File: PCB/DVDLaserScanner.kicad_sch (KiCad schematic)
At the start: 4 parts, among them P1 USB_C_Plug_USB2.0, U3 MIC5365-3.3YC5

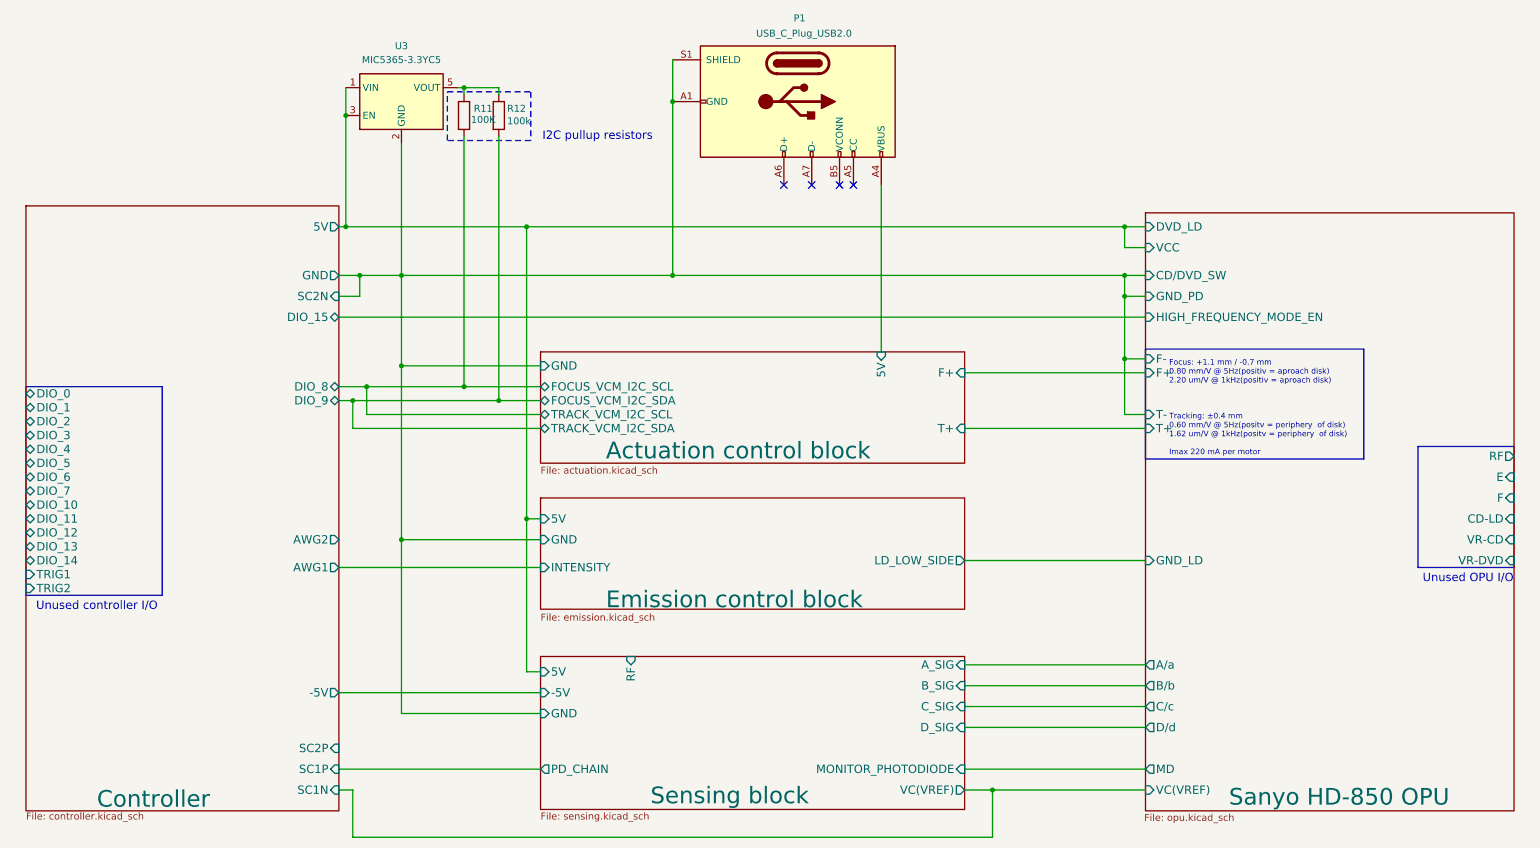
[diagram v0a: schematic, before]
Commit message: Update schematic based on testing
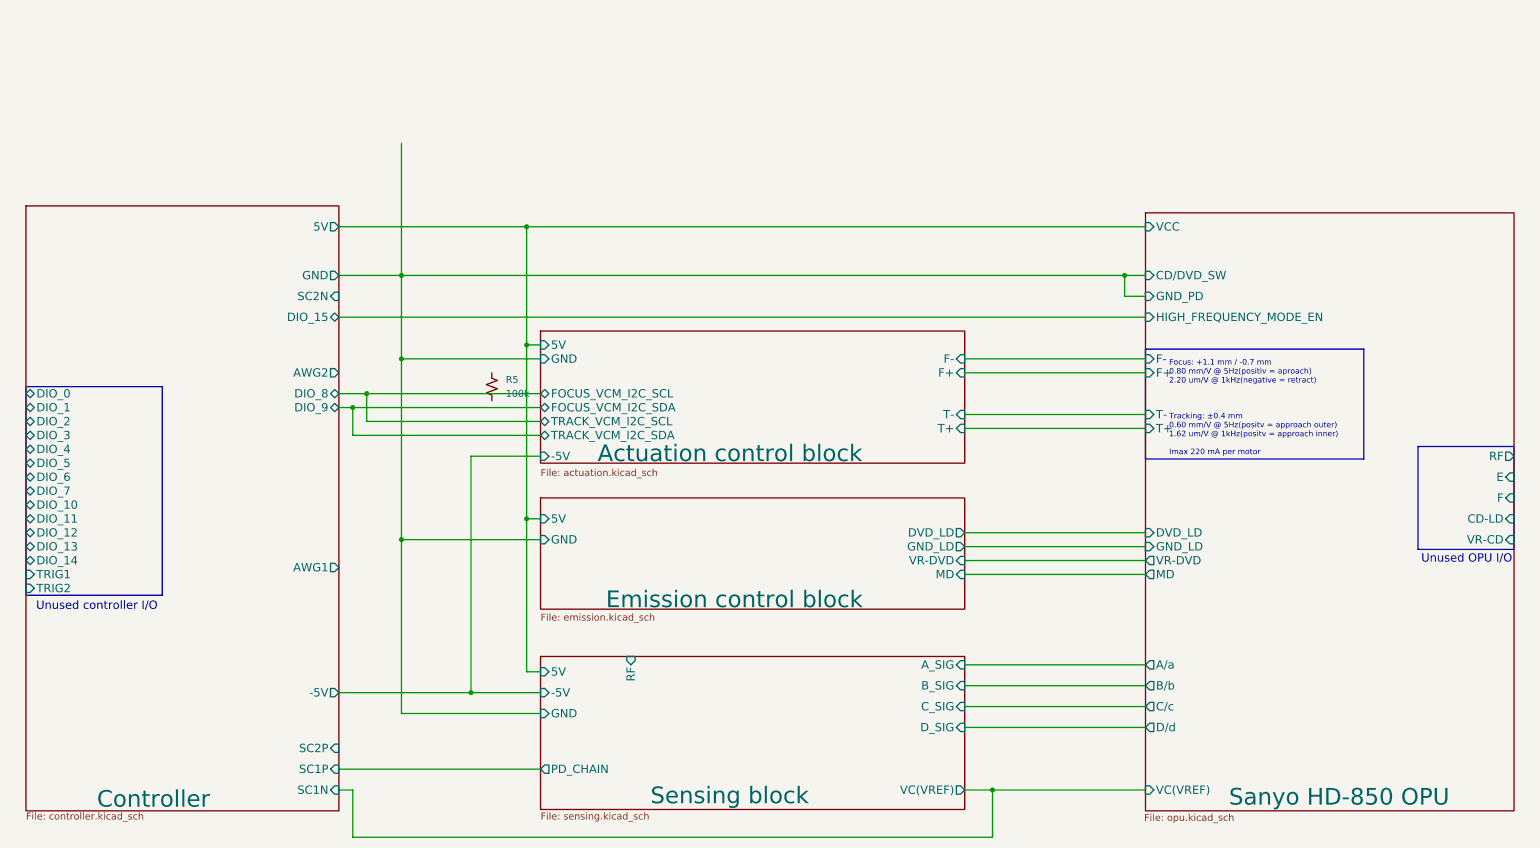
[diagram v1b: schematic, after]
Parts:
- removed P1: USB_C_Plug_USB2.0, symbol Connector:USB_C_Plug_USB2.0
- removed R11: 100K, symbol Device:R
- removed R12: 100k, symbol Device:R
- removed U3: MIC5365-3.3YC5, Package_TO_SOT_SMD:SOT-353_SC-70-5, symbol Regulator_Linear:MIC5365-3.3YC5
- added R5: 100k, symbol Device:R_Small_US
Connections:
- no-connect marks 4 -> 0
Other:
- sheet Actuation control block ports: added -5V, F-, T-; removed none
- sheet Emission control block ports: added DVD_LD, GND_LD, MD, VR-DVD; removed INTENSITY, LD_LOW_SIDE
- sheet Sensing block ports: added none; removed MONITOR_PHOTODIODE
- note added: "Focus: +1.1 mm / -0.7 mm 0.80 mm/V @ 5Hz(positiv = aproach) 2.20 um/V @ 1kHz(negative = retract) Tracking: ±0.4 mm 0.60 mm/V @ 5Hz(positv = approach outer) 1.62 um/V @ 1kHz(positv = approach inner) Imax 220 mA per motor"
- note removed: "Focus: +1.1 mm / -0.7 mm 0.80 mm/V @ 5Hz(positiv = aproach disk) 2.20 um/V @ 1kHz(positiv = aproach disk) Tracking: ±0.4 mm 0.60 mm/V @ 5Hz(positv = periphery of disk) 1.62 um/V @ 1kHz(positv = periphery of disk) Imax 220 mA per motor"
- note removed: "I2C pullup resistors"
